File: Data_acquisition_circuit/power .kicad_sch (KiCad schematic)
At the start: 2 parts, among them U7 LM2596S-5

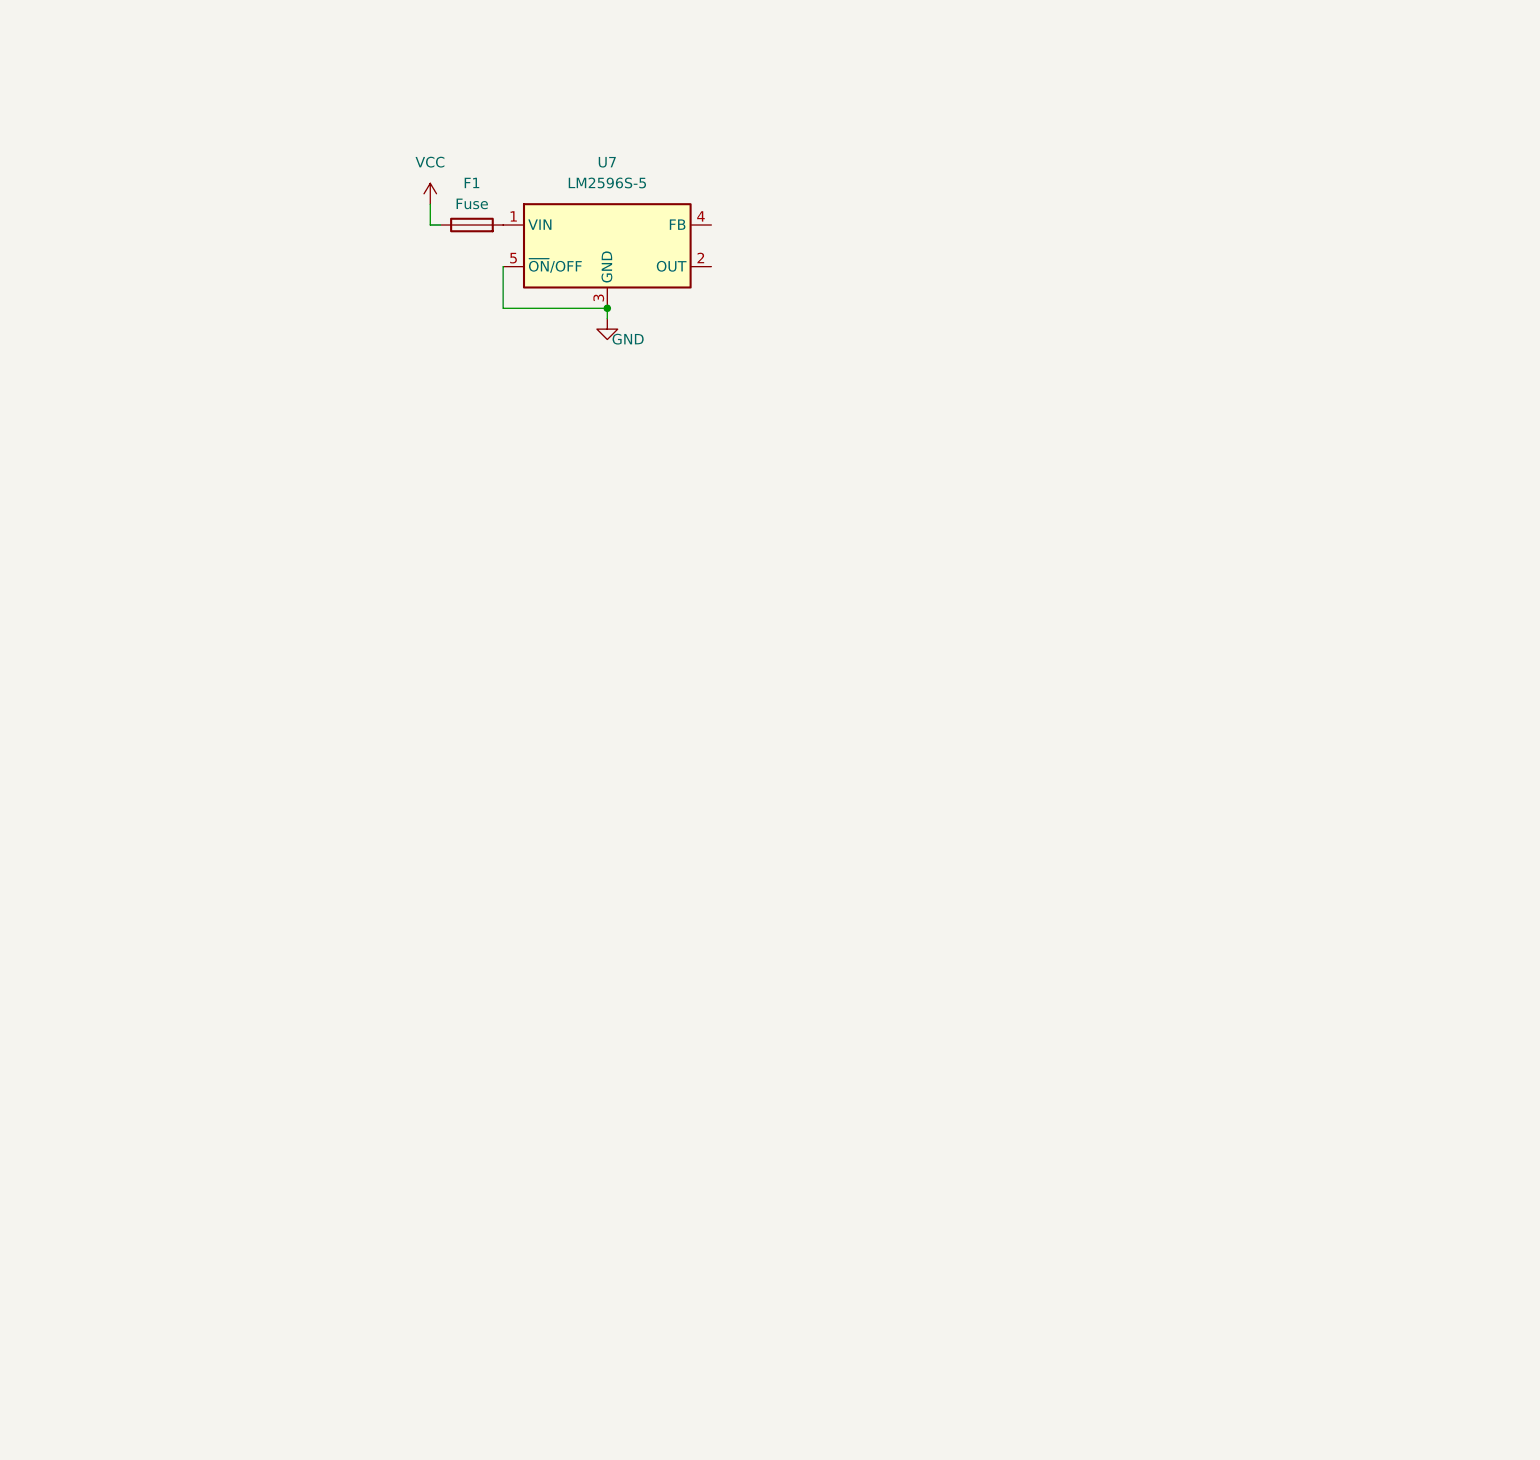
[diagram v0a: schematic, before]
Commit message: covert 0603 to 0805
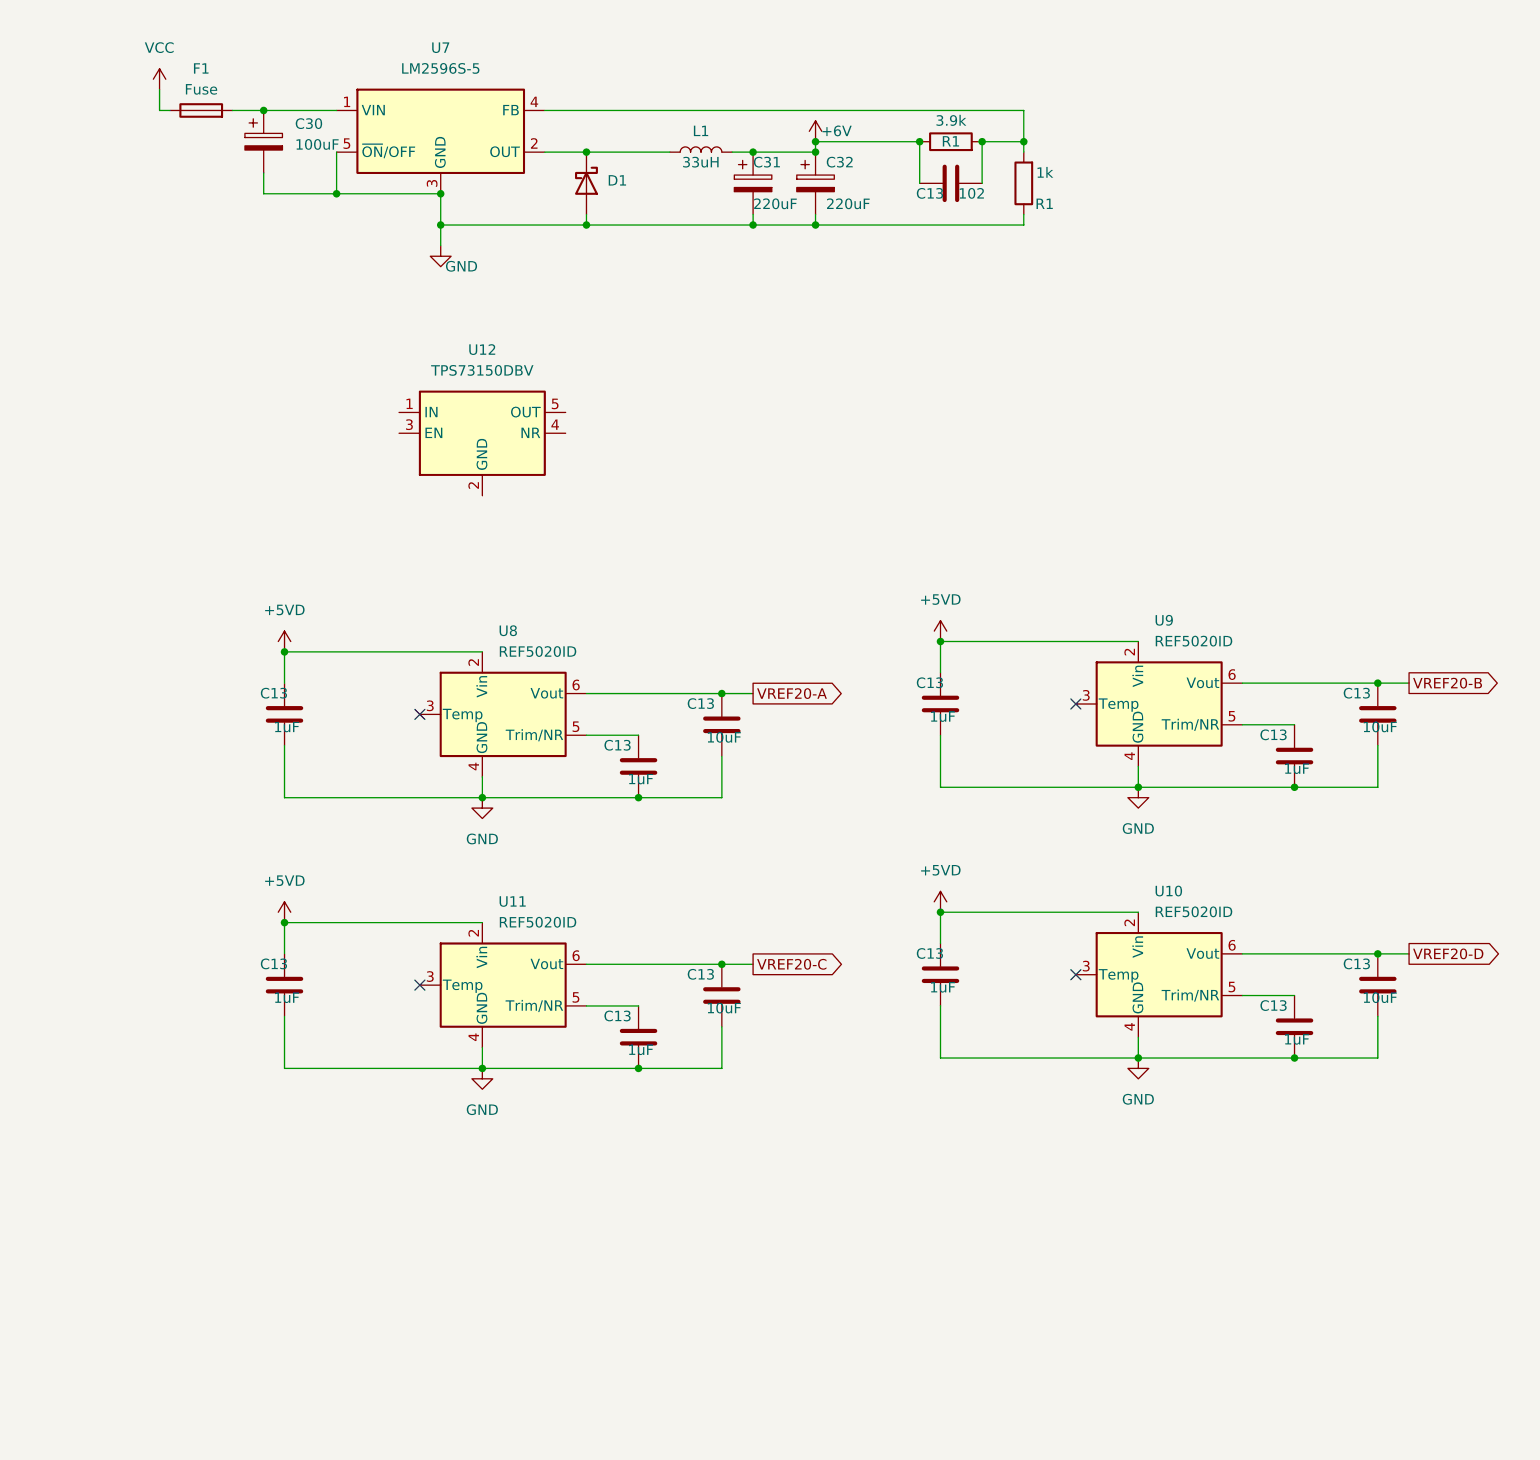
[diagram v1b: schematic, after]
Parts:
- added C13 (x8): 1uF, symbol Device:C
- added C13 (x4): 10uF, symbol Device:C
- added C13: 102, symbol Device:C
- added C30: 100uF, symbol Device:C_Polarized
- added C31, C32: 220uF, symbol Device:C_Polarized
- added D1: 1N5822, Diode_THT:D_DO-201AD_P15.24mm_Horizontal, symbol Diode:1N5822
- added L1: 33uH, symbol Device:L
- added R1: 3.9k, symbol Device:R
- added R1: 1k, symbol Device:R
- added U10, U11, U8, U9: REF5020ID, Package_SO:SOIC-8_3.9x4.9mm_P1.27mm, symbol Reference_Voltage:REF5020ID
- added U12: TPS73150DBV, Package_TO_SOT_SMD:SOT-23-5, symbol Regulator_Linear:TPS73150DBV
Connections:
- net GND: now also C13.1, C13.1, C13.1, C13.1, C13.1, C13.1, C13.1, C13.1, C13.1, C13.1, C13.1, C13.1, C30.2, C31.2, C32.2, D1.2 (A), R1.1, U10.4 (GND), U11.4 (GND), U8.4 (GND), U9.4 (GND)
- net at F1.2, U7.1 (VIN): now also C30.1
- net at U7.2 (OUT): now also D1.1 (K), L1.1
- net at U7.4 (FB): now also C13.1, R1.2, R1.2
- new net: C13.2, U11.5 (Trim/NR)
- new net: C13.2, U10.5 (Trim/NR)
- new net: C13.2, U9.5 (Trim/NR)
- new net: C13.2, U8.5 (Trim/NR)
- new net +5VD: C13.2, C13.2, C13.2, C13.2, U10.2 (Vin), U11.2 (Vin), U8.2 (Vin), U9.2 (Vin)
- new net +6V: C13.2, C31.1, C32.1, L1.2, R1.1
- new net VREF20-A: C13.2, U8.6 (Vout)
- new net VREF20-B: C13.2, U9.6 (Vout)
- new net VREF20-C: C13.2, U11.6 (Vout)
- new net VREF20-D: C13.2, U10.6 (Vout)
- no-connect marks 0 -> 4
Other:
- moved on the sheet: F1, U7

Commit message: add amplifier, adc and rewrite power file
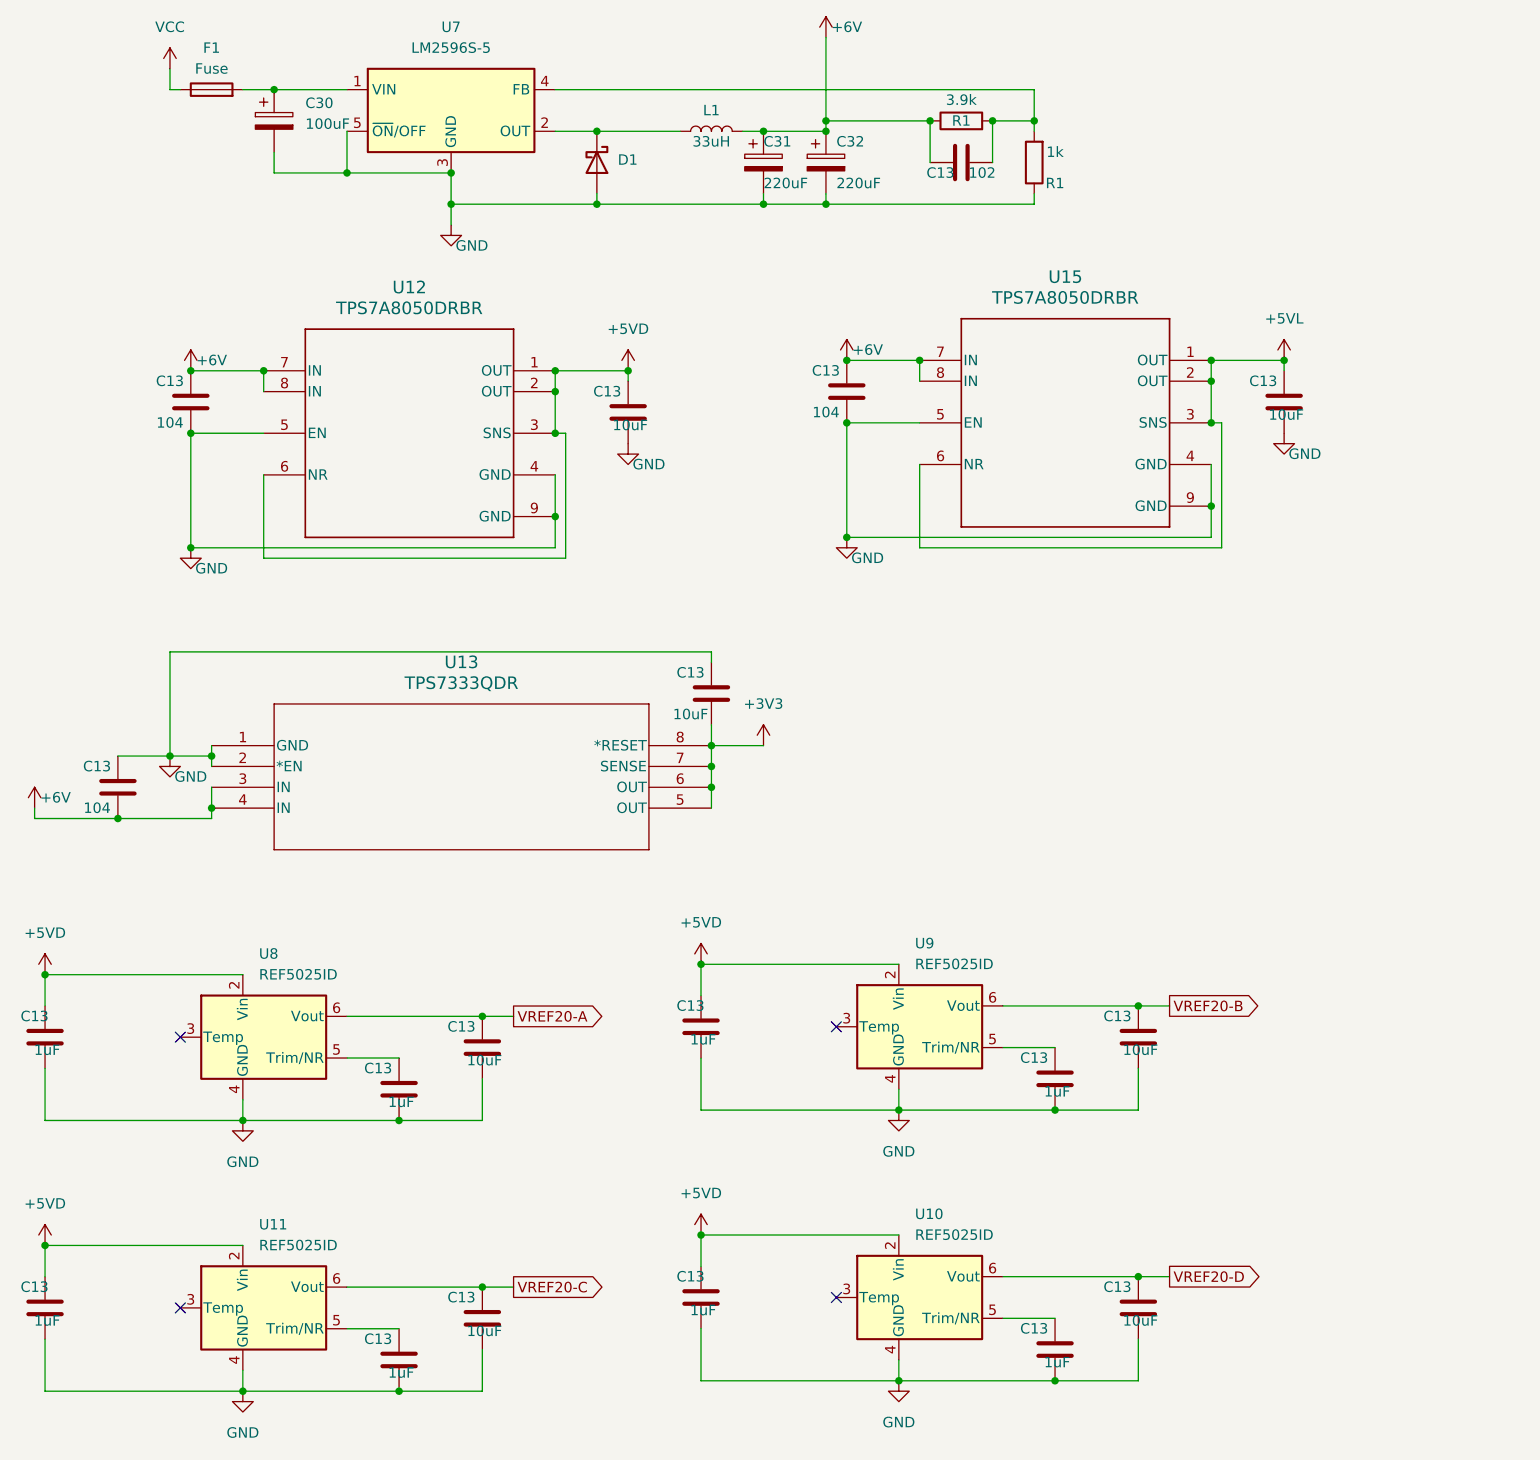
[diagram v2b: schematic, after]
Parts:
- removed U12: TPS73150DBV, Package_TO_SOT_SMD:SOT-23-5, symbol Regulator_Linear:TPS73150DBV
- added C13 (x3): 10uF, symbol Device:C
- added C13 (x3): 104, symbol Device:C
- added U12, U15: TPS7A8050DRBR, DRB0008A-MFG, symbol TPS7A8050DRBR:TPS7A8050DRBR
- added U13: TPS7333QDR, D8_TEX, symbol TPS7333DQR:TPS7333QDR
- U10, U11, U8, U9: value REF5020ID -> REF5025ID
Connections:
- net +5VD: now also C13.2, U12.1 (OUT), U12.2 (OUT), U12.3 (SNS), U12.6 (NR)
- net +6V: now also C13.1, C13.2, C13.2, U12.7 (IN), U12.8 (IN), U13.3 (IN), U13.4 (IN), U15.7 (IN), U15.8 (IN)
- net GND: now also C13.1, C13.1, C13.1, C13.1, C13.2, C13.2, U12.4 (GND), U12.5 (EN), U12.9 (GND), U13.1 (GND), U13.2 (*EN), U15.4 (GND), U15.5 (EN), U15.9 (GND)
- new net +3V3: C13.1, U13.5 (OUT), U13.6 (OUT), U13.7 (SENSE), U13.8 (*RESET)
- new net +5VL: C13.2, U15.1 (OUT), U15.2 (OUT), U15.3 (SNS), U15.6 (NR)
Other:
- moved on the sheet: C13, C30, C31, C32, D1, F1, L1, R1, U10, U11, U7, U8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
